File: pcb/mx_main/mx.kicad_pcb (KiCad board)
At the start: 2 copper layers, 134.9 x 111.5 mm, 63 parts, among them SW1 SW_PUSH, SW10 SW_PUSH, SW11 SW_PUSH, SW12 SW_PUSH, SW13 SW_PUSH, SW14 SW_PUSH, SW15 SW_PUSH, SW16 SW_PUSH, SW17 SW_PUSH, SW18 SW_PUSH, SW19 SW_PUSH, SW2 SW_PUSH, SW20 SW_PUSH, SW21 SW_PUSH, SW22 SW_PUSH, SW23 SW_PUSH, SW24 SW_PUSH, SW25 SW_PUSH, SW26 SW_PUSH, SW27 SW_PUSH, SW28 SW_PUSH, SW29 SW_PUSH, SW3 SW_PUSH, SW30 SW_PUSH, SW32 SW_SPDT, SW4 SW_PUSH, SW5 SW_PUSH, SW6 SW_PUSH, SW7 SW_PUSH, SW8 SW_PUSH, SW9 SW_PUSH

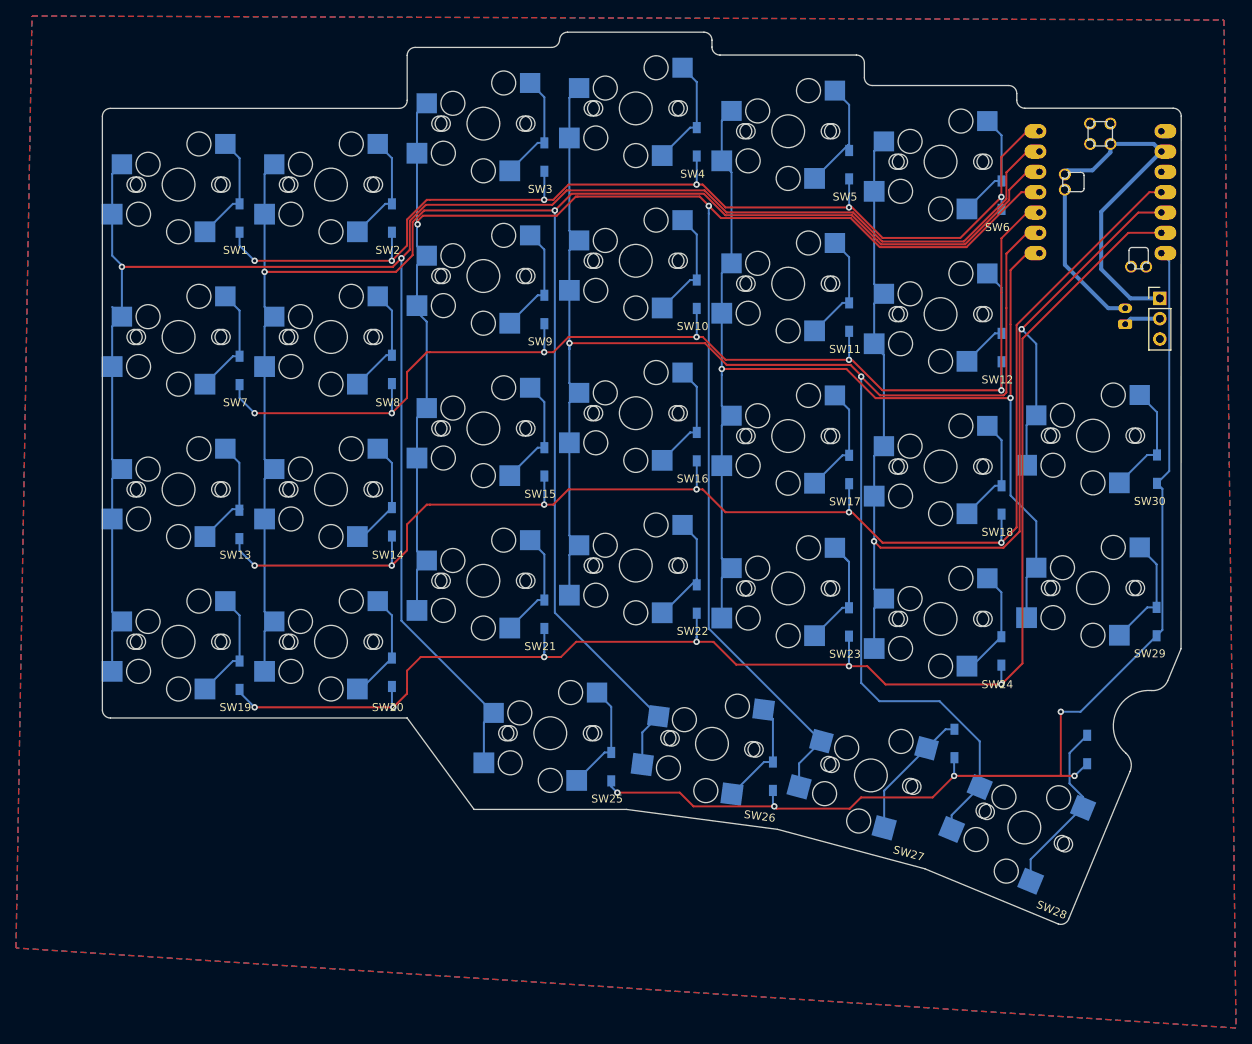
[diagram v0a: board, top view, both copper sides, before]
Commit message: feat: order-ready MX boards (phi 5 centre holes), separate left / right plates, case updates
- PCBs: switch centre holes phi 4.1 -> 5 for Kailh Choc v2 (centre_hole.py); the tracks that fell
  inside the new hole clearance are rerouted by centre_reroute.py (grid A*, vias where one layer is
  full). DRC errors unchanged, 0 unconnected, schematic parity as before.
- SW32 stays a 3-pin THT footprint (2.54 mm); the case's knob opening follows its middle pin
  (SW_Y -54.86) and the finger scoop sits 1 mm toward +y to avoid a thin wall at the MCU block.
- Plates: one per side (pcb/mx_left_plate, pcb/mx_right_tb_plate) instead of the shared
  breakaway plate; 1.2 mm 3MFs for test prints.
- Top case: chamfer on the top outer edge (top_chamfer); machinability probe fix.
- Regenerated specs, 3MFs and MCU cover DXFs; all four documents pass check.py,
  check_parts.py and machinability.py.

Co-Authored-By: Claude Opus 5.5 <noreply@anthropic.com>
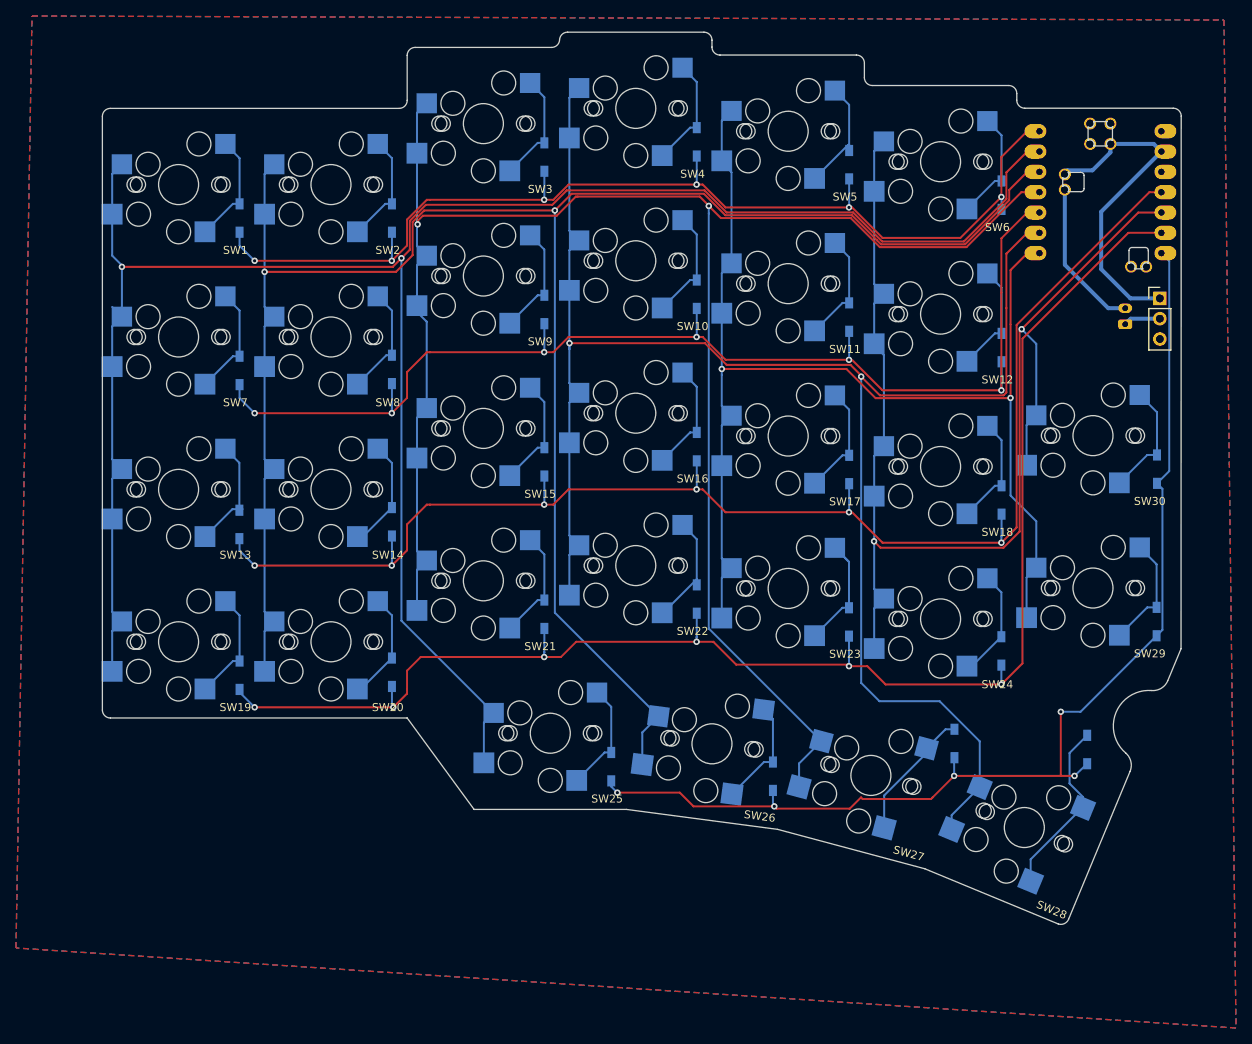
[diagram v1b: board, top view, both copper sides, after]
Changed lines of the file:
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@@
 		(pad "" np_thru_hole circle
 			(at 0 0 90)
-			(size 4.1 4.1)
-			(drill 4.1)
+			(size 5 5)
+			(drill 5)
 			(layers "*.Cu" "*.Mask")
 		)
@@
 		(pad "" np_thru_hole circle
 			(at 0 0 90)
-			(size 4.1 4.1)
-			(drill 4.1)
+			(size 5 5)
+			(drill 5)
 			(layers "*.Cu" "*.Mask")
 		)
@@
 		(pad "" np_thru_hole circle
 			(at 0 0 90)
-			(size 4.1 4.1)
-			(drill 4.1)
+			(size 5 5)
+			(drill 5)
 			(layers "*.Cu" "*.Mask")
 		)
@@
 		(pad "" np_thru_hole circle
 			(at 0 0 90)
-			(size 4.1 4.1)
-			(drill 4.1)
+			(size 5 5)
+			(drill 5)
 			(layers "*.Cu" "*.Mask")
 		)
@@
 		(pad "" np_thru_hole circle
 			(at 0 0 90)
-			(size 4.1 4.1)
-			(drill 4.1)
+			(size 5 5)
+			(drill 5)
 			(layers "*.Cu" "*.Mask")
 		)
@@
 		(pad "" np_thru_hole circle
 			(at 0 0 90)
-			(size 4.1 4.1)
-			(drill 4.1)
+			(size 5 5)
+			(drill 5)
 			(layers "*.Cu" "*.Mask")
 		)
@@
 		(pad "" np_thru_hole circle
 			(at 0 0 90)
-			(size 4.1 4.1)
-			(drill 4.1)
+			(size 5 5)
+			(drill 5)
 			(layers "*.Cu" "*.Mask")
 		)
@@
 		(pad "" np_thru_hole circle
 			(at 0 0 90)
-			(size 4.1 4.1)
-			(drill 4.1)
+			(size 5 5)
+			(drill 5)
 			(layers "*.Cu" "*.Mask")
 		)
@@
 		(pad "" np_thru_hole circle
 			(at 0 0 90)
-			(size 4.1 4.1)
-			(drill 4.1)
+			(size 5 5)
+			(drill 5)
 			(layers "*.Cu" "*.Mask")
 		)
@@
 		(pad "" np_thru_hole circle
 			(at 0 0 90)
-			(size 4.1 4.1)
-			(drill 4.1)
+			(size 5 5)
+			(drill 5)
 			(layers "*.Cu" "*.Mask")
 		)
@@
 		(pad "" np_thru_hole circle
 			(at 0 0 90)
-			(size 4.1 4.1)
-			(drill 4.1)
+			(size 5 5)
+			(drill 5)
 			(layers "*.Cu" "*.Mask")
 		)
@@
 		(pad "" np_thru_hole circle
 			(at 0 0 90)
-			(size 4.1 4.1)
-			(drill 4.1)
+			(size 5 5)
+			(drill 5)
 			(layers "*.Cu" "*.Mask")
 		)
@@
 		(pad "" np_thru_hole circle
 			(at 0 0 90)
-			(size 4.1 4.1)
-			(drill 4.1)
+			(size 5 5)
+			(drill 5)
 			(layers "*.Cu" "*.Mask")
 		)
@@
 		(pad "" np_thru_hole circle
 			(at 0 0 90)
-			(size 4.1 4.1)
-			(drill 4.1)
+			(size 5 5)
+			(drill 5)
 			(layers "*.Cu" "*.Mask")
 		)
@@
 		(pad "" np_thru_hole circle
 			(at 0 0 90)
-			(size 4.1 4.1)
-			(drill 4.1)
+			(size 5 5)
+			(drill 5)
 			(layers "*.Cu" "*.Mask")
 		)
@@
 		(pad "" np_thru_hole circle
 			(at 0 0 90)
-			(size 4.1 4.1)
-			(drill 4.1)
+			(size 5 5)
+			(drill 5)
 			(layers "*.Cu" "*.Mask")
 		)
@@
 		(pad "" np_thru_hole circle
 			(at 0 0 75)
-			(size 4.1 4.1)
-			(drill 4.1)
+			(size 5 5)
+			(drill 5)
 			(layers "*.Cu" "*.Mask")
 		)
@@
 		(pad "" np_thru_hole circle
 			(at 0 0 90)
-			(size 4.1 4.1)
-			(drill 4.1)
+			(size 5 5)
+			(drill 5)
 			(layers "*.Cu" "*.Mask")
 		)
@@
 		(pad "" np_thru_hole circle
 			(at 0 0 90)
-			(size 4.1 4.1)
-			(drill 4.1)
+			(size 5 5)
+			(drill 5)
 			(layers "*.Cu" "*.Mask")
 		)
@@
 		(pad "" np_thru_hole circle
 			(at 0 0 90)
-			(size 4.1 4.1)
-			(drill 4.1)
+			(size 5 5)
+			(drill 5)
 			(layers "*.Cu" "*.Mask")
 		)
@@
 		(pad "" np_thru_hole circle
 			(at 0 0 82.5)
-			(size 4.1 4.1)
-			(drill 4.1)
+			(size 5 5)
+			(drill 5)
 			(layers "*.Cu" "*.Mask")
 		)
@@
 		(pad "" np_thru_hole circle
 			(at 0 0 90)
-			(size 4.1 4.1)
-			(drill 4.1)
+			(size 5 5)
+			(drill 5)
 			(layers "*.Cu" "*.Mask")
 		)
@@
 		(pad "" np_thru_hole circle
 			(at 0 0 90)
-			(size 4.1 4.1)
-			(drill 4.1)
+			(size 5 5)
+			(drill 5)
 			(layers "*.Cu" "*.Mask")
 		)
@@
 		(pad "" np_thru_hole circle
 			(at 0 0 90)
-			(size 4.1 4.1)
-			(drill 4.1)
+			(size 5 5)
+			(drill 5)
 			(layers "*.Cu" "*.Mask")
 		)
@@
 		(pad "" np_thru_hole circle
 			(at 0 0 90)
-			(size 4.1 4.1)
-			(drill 4.1)
+			(size 5 5)
+			(drill 5)
 			(layers "*.Cu" "*.Mask")
 		)
@@
 		(pad "" np_thru_hole circle
 			(at 0 0 90)
-			(size 4.1 4.1)
-			(drill 4.1)
+			(size 5 5)
+			(drill 5)
 			(layers "*.Cu" "*.Mask")
 		)
@@
 		(pad "" np_thru_hole circle
 			(at 0 0 67.5)
-			(size 4.1 4.1)
-			(drill 4.1)
+			(size 5 5)
+			(drill 5)
 			(layers "*.Cu" "*.Mask")
 		)
@@
 		(pad "" np_thru_hole circle
 			(at 0 0 90)
-			(size 4.1 4.1)
-			(drill 4.1)
+			(size 5 5)
+			(drill 5)
 			(layers "*.Cu" "*.Mask")
 		)
@@
 		(pad "" np_thru_hole circle
 			(at 0 0 90)
-			(size 4.1 4.1)
-			(drill 4.1)
+			(size 5 5)
+			(drill 5)
 			(layers "*.Cu" "*.Mask")
 		)
@@
 		(pad "" np_thru_hole circle
 			(at 0 0 90)
-			(size 4.1 4.1)
-			(drill 4.1)
+			(size 5 5)
+			(drill 5)
 			(layers "*.Cu" "*.Mask")
 		)
@@
 	(gr_line
 		(start 177.021746 129.927534)
-		(end 184.707580 111.442916)
+		(end 184.70758 111.442916)
 		(stroke
 			(width 0.1)
@@
 	)
 	(gr_arc
-		(start 184.707580 111.442916)
-		(mid 184.806483 110.211876)
-		(end 184.163497 109.157451)
+		(start 184.163497 109.157451)
+		(mid 184.806521 110.211877)
+		(end 184.70758 111.442916)
 		(stroke
 			(width 0.1)
@@
 	)
 	(gr_arc
-		(start 187.412059 101.344579)
-		(mid 188.613091 101.056890)
-		(end 189.416170 100.118642)
+		(start 189.41617 100.118642)
+		(mid 188.613097 101.056917)
+		(end 187.412059 101.344579)
 		(stroke
 			(width 0.1)
@@
 	)
 	(gr_line
-		(start 189.416170 100.118642)
+		(start 189.41617 100.118642)
 		(end 191.077007 96.124288)
 		(stroke
@@
 	)
 	(segment
-		(start 153.969562 113.858335)
-		(end 159.266779 108.561118)
+		(start 159.2696 109.161099)
+		(end 159.2668 108.5611)
+		(width 0.25)
+		(layer "B.Cu")
+		(net "Net-(D27-A)")
+	)
+	(segment
+		(start 153.9696 118.5091)
+		(end 153.9696 114.4611)
 		(width 0.25)
 		(layer "B.Cu")
@@
 	)
 	(segment
-		(start 162.7555 106.187)
-		(end 161.640897 106.187)
+		(start 153.9696 114.4611)
+		(end 159.2696 109.161099)
 		(width 0.25)
 		(layer "B.Cu")
@@
 	)
 	(segment
-		(start 153.969562 118.509065)
-		(end 153.969562 113.858335)
+		(start 162.7555 106.187)
+		(end 161.640897 106.187)
 		(width 0.25)
 		(layer "B.Cu")
@@
 	)
 	(segment
+		(start 151.278399 114.9055)
+		(end 159.8284 114.9055)
+		(width 0.25)
+		(layer "F.Cu")
+		(net "ROW4")
+	)
+	(segment
 		(start 128.4255 114.109493)
 		(end 130.14 115.823993)
@@
 	)
 	(segment
-		(start 151.078401 114.705504)
-		(end 160.023989 114.705504)
+		(start 151.0784 114.7055)
+		(end 151.278399 114.9055)
+		(width 0.25)
+		(layer "F.Cu")
+		(net "ROW4")
+	)
+	(segment
+		(start 159.8284 114.9055)
+		(end 160.024 114.7055)
 		(width 0.25)
 		(layer "F.Cu")
